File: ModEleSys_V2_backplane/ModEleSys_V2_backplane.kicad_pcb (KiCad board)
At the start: 2 copper layers, 90 x 98 mm, 34 parts, among them J5 Conn_01x03, J6 Conn_01x03

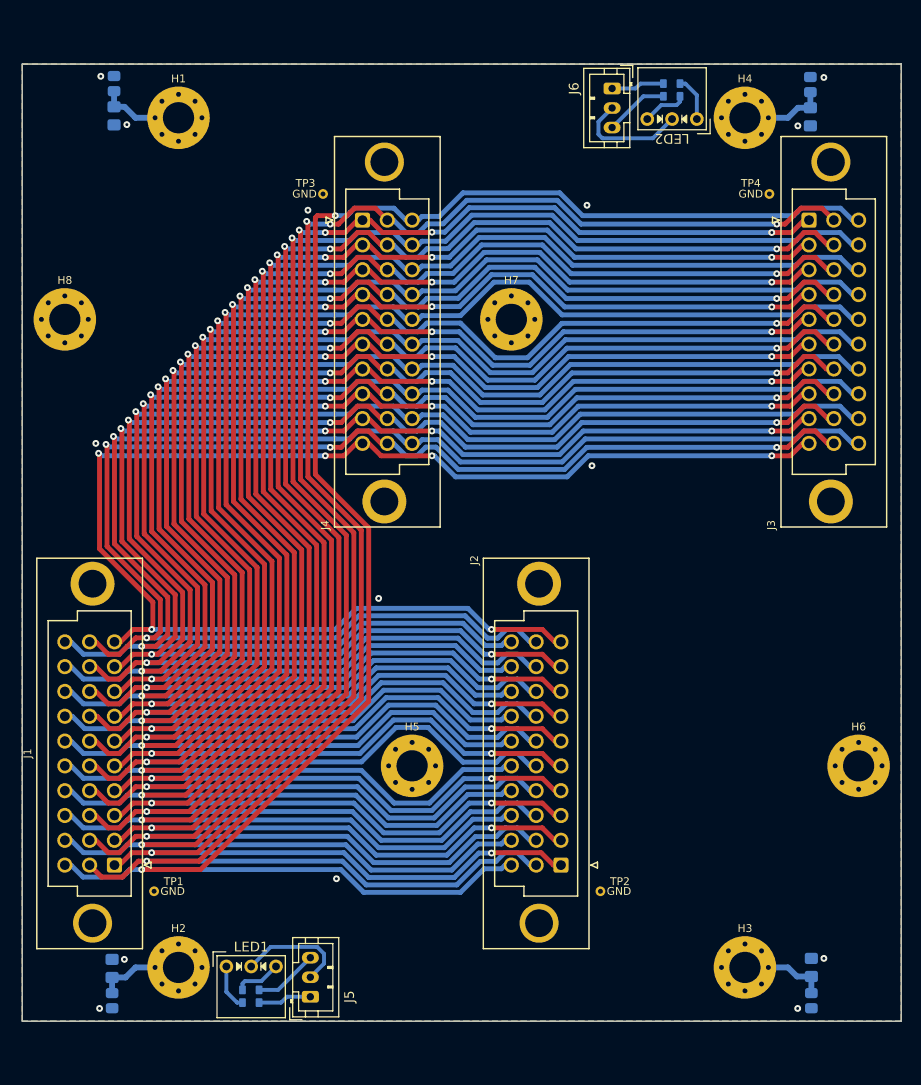
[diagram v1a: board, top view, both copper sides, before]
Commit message: updated and added on off switch
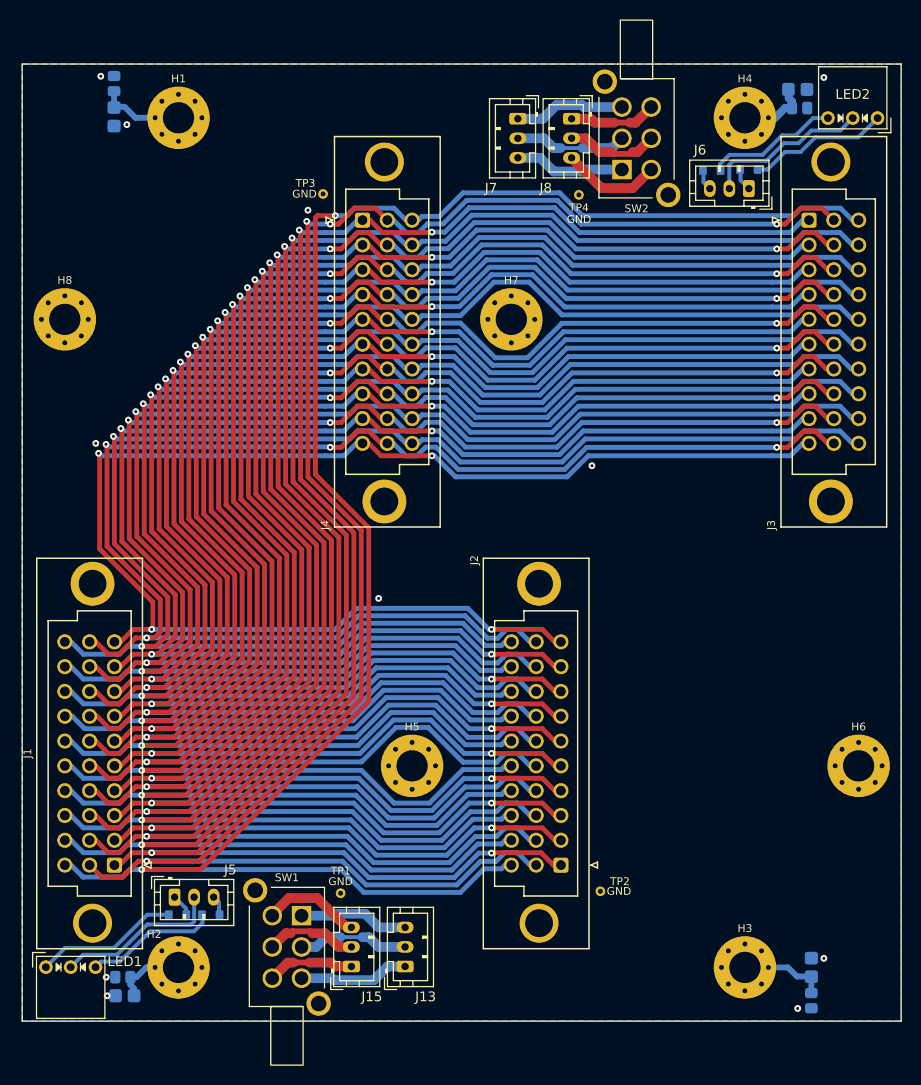
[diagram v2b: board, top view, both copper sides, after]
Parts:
- added J13: Conn_01x03, Connector_JST:JST_PH_B3B-PH-K_1x03_P2.00mm_Vertical, F.Cu at (159.3, 132.3)
- added J15: Conn_01x03, Connector_JST:JST_PH_B3B-PH-K_1x03_P2.00mm_Vertical, F.Cu at (153.8, 132.3)
- added J7: Conn_01x03, Connector_JST:JST_PH_B3B-PH-K_1x03_P2.00mm_Vertical, F.Cu at (170.8, 45.5)
- added J8: Conn_01x03, Connector_JST:JST_PH_B3B-PH-K_1x03_P2.00mm_Vertical, F.Cu at (176.3, 45.5)
- added SW1: switch_DPDT, SquantorSwitches:PS-22F02, F.Cu at (147.2, 130.3)
- added SW2: switch_DPDT, SquantorSwitches:PS-22F02, F.Cu at (183.0, 47.5)
- N2: value V:20240218 -> V:20251015
- R5, R6, R7, R8: footprint SquantorRcl:R_0603_hand -> SquantorResistor:R_0603_hand
- moved TP4 19.5 mm to (177.1, 53.3)
- moved TP1 19.1 mm to (152.7, 124.8)
- moved LED2 18.5 mm to (205.1, 45.4)
- moved LED1 18.5 mm to (125.1, 132.4)
- moved J6 17.4 mm to (194.5, 52.6), turned to 180 degrees
- moved J5 17.2 mm to (135.7, 125.2), turned to 0 degrees
- moved R7 11.8 mm to (194.5, 50.7)
- moved R5 11.7 mm to (136.0, 127.0)
- moved R6 8.72 mm to (139.4, 127.0)
- moved R8 8.64 mm to (190.7, 50.8)
- moved C2 3.09 mm to (130.6, 135.3), turned to 180 degrees
- moved C4 3.09 mm to (199.5, 42.5), turned to 0 degrees
- moved R4 2.64 mm to (199.7, 44.4), turned to 0 degrees
- moved R2 2.64 mm to (130.4, 133.4), turned to 180 degrees
- moved C1 0.10 mm to (129.5, 45.3)
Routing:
- net Net-(J7-Pin_2): track 0.00 -> 11.5 mm
- net Net-(J13-Pin_2): track 0.00 -> 11.4 mm
- net Net-(J7-Pin_3): track 0.00 -> 11.3 mm
- net Net-(J7-Pin_1): track 0.00 -> 11.3 mm
- net Net-(J13-Pin_3): track 0.00 -> 11.3 mm
- net Net-(J13-Pin_1): track 0.00 -> 11.3 mm
- net Net-(J8-Pin_3): track 0.00 -> 10.3 mm
- net Net-(J15-Pin_3): track 0.00 -> 10.1 mm
- net Net-(LED1-A1): track 4.71 -> 14.9 mm
- net Net-(LED2-A1): track 4.67 -> 14.5 mm
- net Net-(J8-Pin_2): track 0.00 -> 9.48 mm
- net Net-(J15-Pin_2): track 0.00 -> 9.43 mm
- net Net-(LED2-A2): track 4.64 -> 13.7 mm
- net Net-(J8-Pin_1): track 0.00 -> 8.98 mm
- net Net-(J15-Pin_1): track 0.00 -> 8.93 mm
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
